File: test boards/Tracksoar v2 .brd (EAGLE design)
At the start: 50.4 x 19.5 mm, 46 parts, among them IC1 BME280, IC2 74AHC1G125DBV, Y1 16MHZ

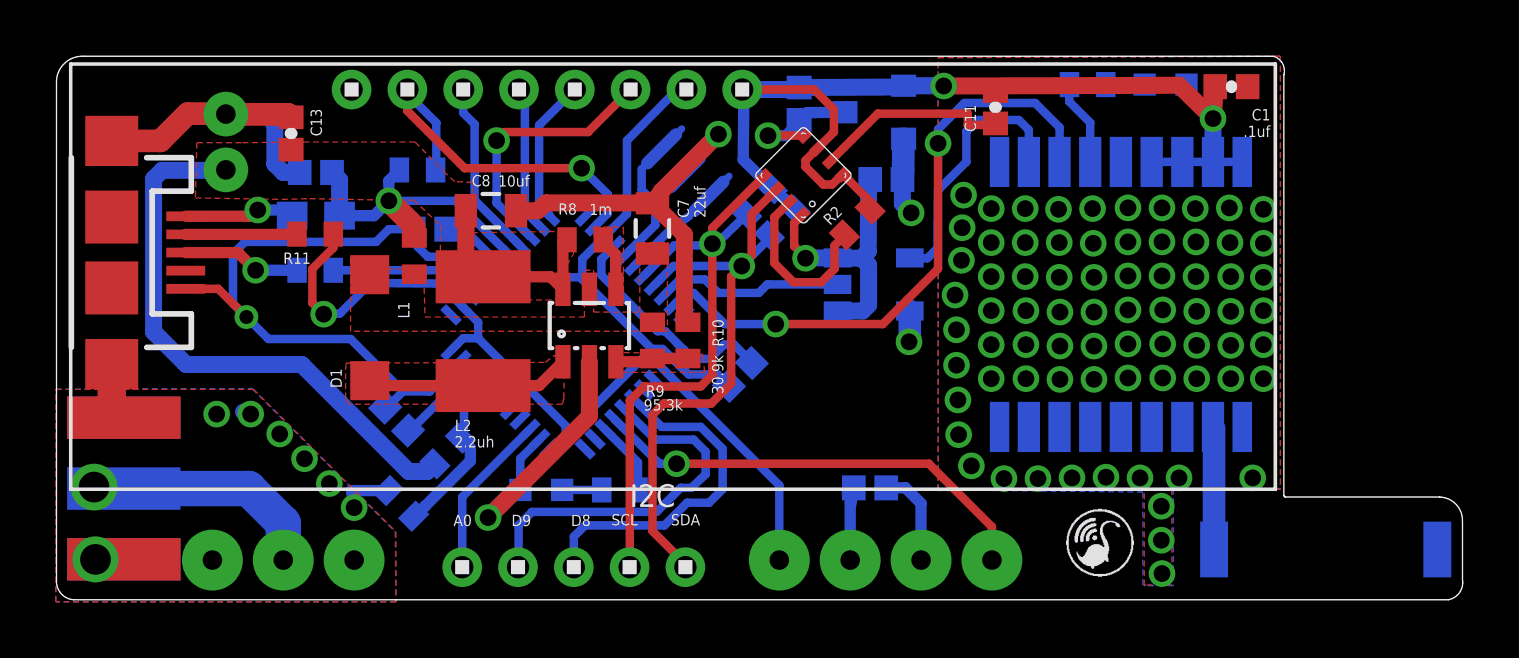
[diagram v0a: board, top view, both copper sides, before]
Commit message: v2 BME280 decoupling cap
added decoupling cap to bme280 of v2 board.
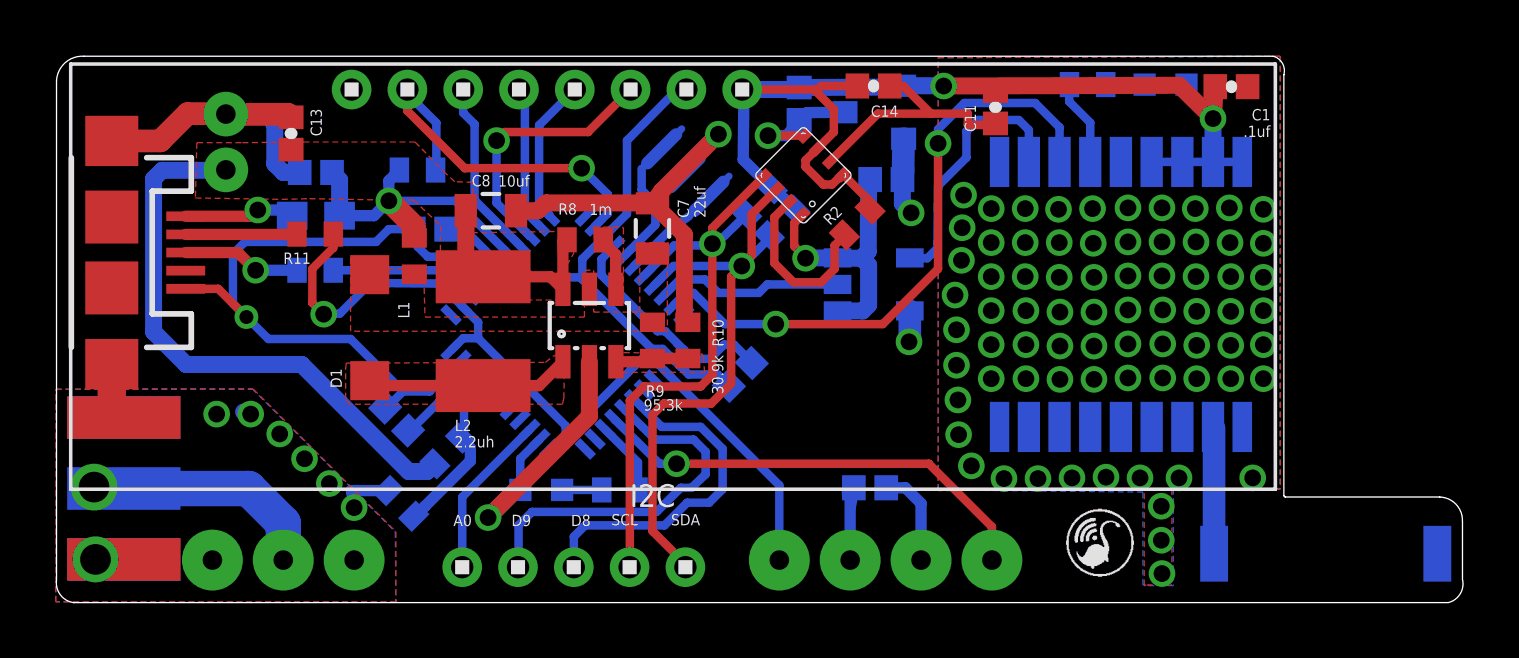
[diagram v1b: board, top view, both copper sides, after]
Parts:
- added C14: .1uf, SparkFun-Capacitors:0402-CAP
- moved GPS-ANT 0.15 mm to (45.5, 1.73)
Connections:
- net 3V: now also C14.2
- net GND: now also C14.1
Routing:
- net GND: track 100.0 -> 101.9 mm
- net 3V: track 39.9 -> 41.5 mm
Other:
- board size 50.4 x 19.5 mm -> 50.4 x 19.6 mm
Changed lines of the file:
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@@
 <layers>
 <layer number="1" name="Top" color="4" fill="1" visible="yes" active="yes"/>
-<layer number="2" name="Route2" color="1" fill="3" visible="no" active="yes"/>
+<layer number="2" name="Route2" color="1" fill="3" visible="yes" active="yes"/>
 <layer number="3" name="Route3" color="4" fill="3" visible="no" active="no"/>
 <layer number="14" name="Route14" color="1" fill="6" visible="no" active="no"/>
-<layer number="15" name="Route15" color="4" fill="6" visible="no" active="yes"/>
+<layer number="15" name="Route15" color="4" fill="6" visible="yes" active="yes"/>
 <layer number="16" name="Bottom" color="1" fill="1" visible="yes" active="yes"/>
 <layer number="17" name="Pads" color="2" fill="1" visible="yes" active="yes"/>
@@
 <rectangle x1="37.1729" y1="3.2893" x2="37.6809" y2="3.3147" layer="25"/>
 <rectangle x1="37.3507" y1="3.3147" x2="37.5031" y2="3.3401" layer="25"/>
-<wire x1="0.635" y1="0.0762" x2="0.0254" y2="0.7874" width="0" layer="20" curve="-90"/>
+<wire x1="0.635" y1="-0.0254" x2="0.0254" y2="0.7874" width="0" layer="20" curve="-90"/>
 <wire x1="0.0254" y1="0.7874" x2="0.0254" y2="18.6944" width="0" layer="20"/>
 <wire x1="0.0254" y1="18.6944" x2="1.016" y2="19.558" width="0" layer="20" curve="-90"/>
@@
 <wire x1="49.6062" y1="3.7592" x2="50.419" y2="2.8956" width="0" layer="20" curve="-90"/>
 <wire x1="50.419" y1="2.8956" x2="50.419" y2="0.8128" width="0" layer="20"/>
-<wire x1="50.419" y1="0.8128" x2="49.911" y2="0.0762" width="0" layer="20" curve="-90"/>
-<wire x1="49.911" y1="0.0762" x2="0.635" y2="0.0762" width="0" layer="20"/>
+<wire x1="50.419" y1="0.8128" x2="49.911" y2="-0.0254" width="0" layer="20" curve="-90"/>
+<wire x1="49.911" y1="-0.0254" x2="0.635" y2="-0.0254" width="0" layer="20"/>
 <text x="29.9212" y="9.1694" size="0.4064" layer="26" rot="MR0">74AHC1G125</text>
 <text x="14.2494" y="2.7178" size="0.4064" layer="25">A0</text>
@@
 <attribute name="VALUE" x="15.8496" y="14.8844" size="0.4064" layer="25"/>
 </element>
-<element name="GPS-ANT" library="SparkFun-RF" package="ANTENNA-CHIP4" value="ANTENNA2SMD3" x="45.5168" y="1.8796" smashed="yes" rot="MR180">
-<attribute name="NAME" x="44.778" y="3.5154" size="0.4064" layer="26" rot="MR180"/>
+<element name="GPS-ANT" library="SparkFun-RF" package="ANTENNA-CHIP4" value="ANTENNA2SMD3" x="45.5168" y="1.7272" smashed="yes" rot="MR180">
+<attribute name="NAME" x="44.778" y="3.363" size="0.4064" layer="26" rot="MR180"/>
 </element>
 <element name="FTDI" library="headers(2mm)" package="1X8" value="1X8" x="17.6022" y="18.3642" rot="R180"/>
@@
 <element name="C12" library="SparkFun-Capacitors" package="0402-CAP" value="1uf" x="12.2174" y="6.5532" rot="MR225"/>
 <element name="C13" library="SparkFun-Capacitors" package="0402-CAP" value=".1uf" x="8.4328" y="16.7894" rot="R270"/>
+<element name="C14" library="SparkFun-Capacitors" package="0402-CAP" value=".1uf" x="29.3116" y="18.4912" rot="R180"/>
 </elements>
 <signals>
@@
 <wire x1="21.2454" y1="14.3002" x2="21.3868" y2="14.2858" width="0.6096" layer="1"/>
 <wire x1="27.75159375" y1="15.785771875" x2="29.466421875" y2="17.5006" width="0.3048" layer="1"/>
-<wire x1="29.466421875" y1="17.5006" x2="32.6898" y2="17.5006" width="0.3048" layer="1"/>
+<wire x1="29.466421875" y1="17.5006" x2="31.369" y2="17.5006" width="0.3048" layer="1"/>
+<wire x1="31.369" y1="17.5006" x2="32.6898" y2="17.5006" width="0.3048" layer="1"/>
 <wire x1="32.6898" y1="17.5006" x2="32.6898" y2="17.0942" width="0.3048" layer="1"/>
 <wire x1="32.6898" y1="17.0942" x2="33.6804" y2="17.0942" width="0.3048" layer="1"/>
@@
 <wire x1="6.7056" y1="17.4752" x2="6.6962" y2="17.4846" width="0.8128" layer="1"/>
 <wire x1="6.6962" y1="17.4846" x2="6.096" y2="17.4846" width="0.8128" layer="1"/>
+<contactref element="C14" pad="1"/>
+<wire x1="29.8916" y1="18.4912" x2="30.3784" y2="18.4912" width="0.3048" layer="1"/>
+<wire x1="30.3784" y1="18.4912" x2="31.369" y2="17.5006" width="0.3048" layer="1"/>
 <wire x1="22.5298" y1="10.0226" x2="21.844" y2="9.7028" width="0" layer="19" extent="1-16"/>
 </signal>
@@
 <wire x1="30.3878" y1="16.6014" x2="30.368" y2="15.402" width="0.8128" layer="16"/>
 <wire x1="30.5816" y1="9.3218" x2="30.6324" y2="9.271" width="0.8128" layer="15"/>
-<wire x1="25.146" y1="6.3754" x2="25.5524" y2="6.3754" width="0.3048" layer="15"/>
 <wire x1="30.6116" y1="10.4292" x2="30.6116" y2="9.3518" width="0.8128" layer="16"/>
 <wire x1="30.6116" y1="9.3518" x2="30.5816" y2="9.3218" width="0.8128" layer="16"/>
@@
 <wire x1="27.291971875" y1="16.24539375" x2="27.8892" y2="16.842621875" width="0.3048" layer="1"/>
 <wire x1="27.8892" y1="16.842621875" x2="27.8892" y2="17.653" width="0.3048" layer="1"/>
-<wire x1="27.8892" y1="17.653" x2="27.178" y2="18.3642" width="0.3048" layer="1"/>
+<wire x1="27.8892" y1="17.653" x2="27.2415" y2="18.3007" width="0.3048" layer="1"/>
+<wire x1="27.2415" y1="18.3007" x2="27.178" y2="18.3642" width="0.3048" layer="1"/>
 <wire x1="27.178" y1="18.3642" x2="24.6022" y2="18.3642" width="0.3048" layer="1"/>
 <wire x1="41.5586" y1="18.4658" x2="41.4886" y2="17.3332" width="0.6096" layer="1"/>
@@
 <wire x1="31.8262" y1="18.4912" x2="33.5938" y2="18.4912" width="0.4064" layer="1"/>
 <wire x1="33.5938" y1="18.4912" x2="33.6804" y2="18.3092" width="0.4064" layer="1"/>
+<contactref element="C14" pad="2"/>
+<wire x1="28.7316" y1="18.4912" x2="27.432" y2="18.4912" width="0.3048" layer="1"/>
+<wire x1="27.432" y1="18.4912" x2="27.2415" y2="18.3007" width="0.3048" layer="1"/>
 </signal>
 <signal name="N$1">
@@
 <wire x1="34.5186" y1="17.272" x2="33.0454" y2="17.272" width="0.3048" layer="16"/>
 <wire x1="33.0454" y1="17.272" x2="32.639" y2="16.8656" width="0.3048" layer="16"/>
-<wire x1="32.639" y1="16.8656" x2="32.639" y2="15.7734" width="0.3048" layer="16"/>
-<wire x1="32.639" y1="15.7734" x2="31.623" y2="14.7574" width="0.3048" layer="16"/>
-<wire x1="31.623" y1="14.7574" x2="31.5976" y2="12.6746" width="0.3048" layer="16"/>
+<wire x1="32.639" y1="16.8656" x2="32.639" y2="15.9258" width="0.3048" layer="16"/>
+<wire x1="32.639" y1="15.9258" x2="31.623" y2="14.9098" width="0.3048" layer="16"/>
+<wire x1="31.623" y1="14.9098" x2="31.5976" y2="12.6746" width="0.3048" layer="16"/>
 <wire x1="31.5976" y1="12.6746" x2="31.242" y2="12.319" width="0.3048" layer="16"/>
 <wire x1="31.242" y1="12.319" x2="30.6218" y2="12.319" width="0.3048" layer="16"/>
@@
 <contactref element="GPS-ANT" pad="SIG"/>
 <wire x1="41.477" y1="6.2704" x2="41.5168" y2="6.2306" width="0.3048" layer="16"/>
-<wire x1="41.5168" y1="6.2306" x2="41.5168" y2="1.8796" width="0.8128" layer="16"/>
+<wire x1="41.5168" y1="6.2306" x2="41.5168" y2="1.7272" width="0.8128" layer="16"/>
 </signal>
 <signal name="PPS">

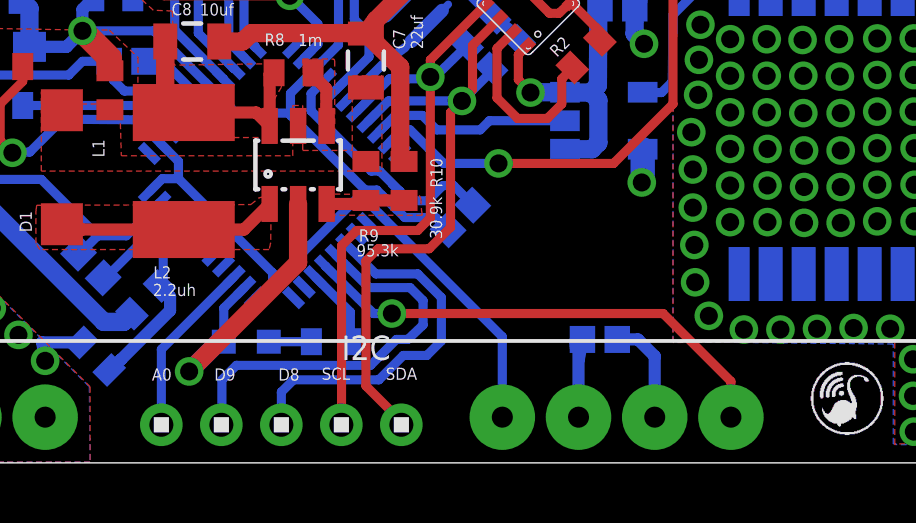
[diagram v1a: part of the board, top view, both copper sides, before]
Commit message: Added Pull down to HWB pin
added a 10k pull down resistor to HWB to resolve issues flashing the
boot loader
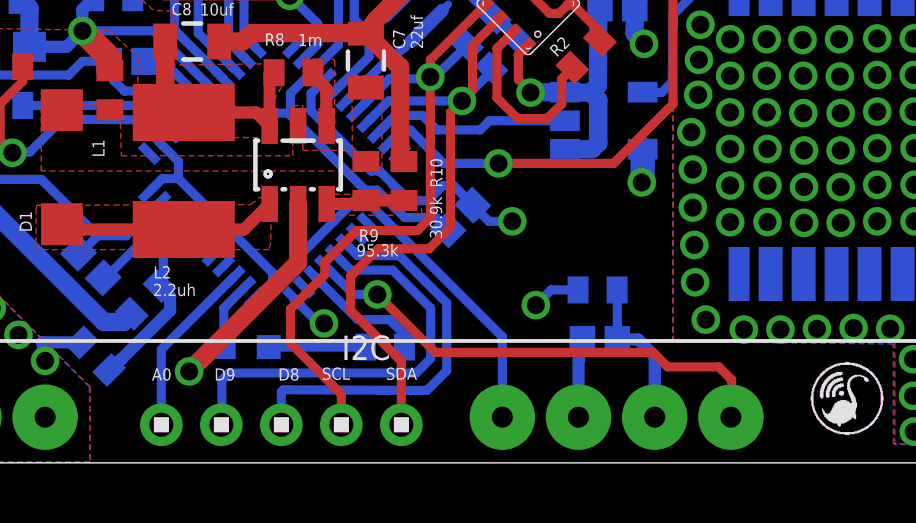
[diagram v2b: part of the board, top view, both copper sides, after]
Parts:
- added R12: 10k, adafruit:R0402
- moved R6 1.81 mm to (22.0, 3.84)
- moved PTT 0.18 mm to (17.4, 3.84)
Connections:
- new net HWB: R12.2, U$4.33
- net GND: now also R12.1
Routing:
- net HWB: track 0.00 -> 10.8 mm, vias 0 -> 2
- net GND: track 101.9 -> 106.1 mm, vias 85 -> 86
- net N$27: track 1.42 -> 3.22 mm
- net LED: track 2.67 -> 4.21 mm
- net SCL: track 21.8 -> 23.2 mm
- net D9: track 13.3 -> 14.3 mm
- net D8: track 12.5 -> 13.3 mm
- net SDA: track 21.8 -> 22.3 mm
